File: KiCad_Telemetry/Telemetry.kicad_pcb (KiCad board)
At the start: 2 copper layers, 67 x 51 mm, 38 parts, among them IC1 TCAN1044VDRQ1, J2 Conn_01x03, J3 PinHeader_01x02, J4 PinHeader_01x02, J5 PinHeader_01x02, J7 DB9_Female, J8 USB_A Connector, U1 NRF24L01_Breakout, U2 STM32F042C4T6, U3 TLV70033_SOT23-5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

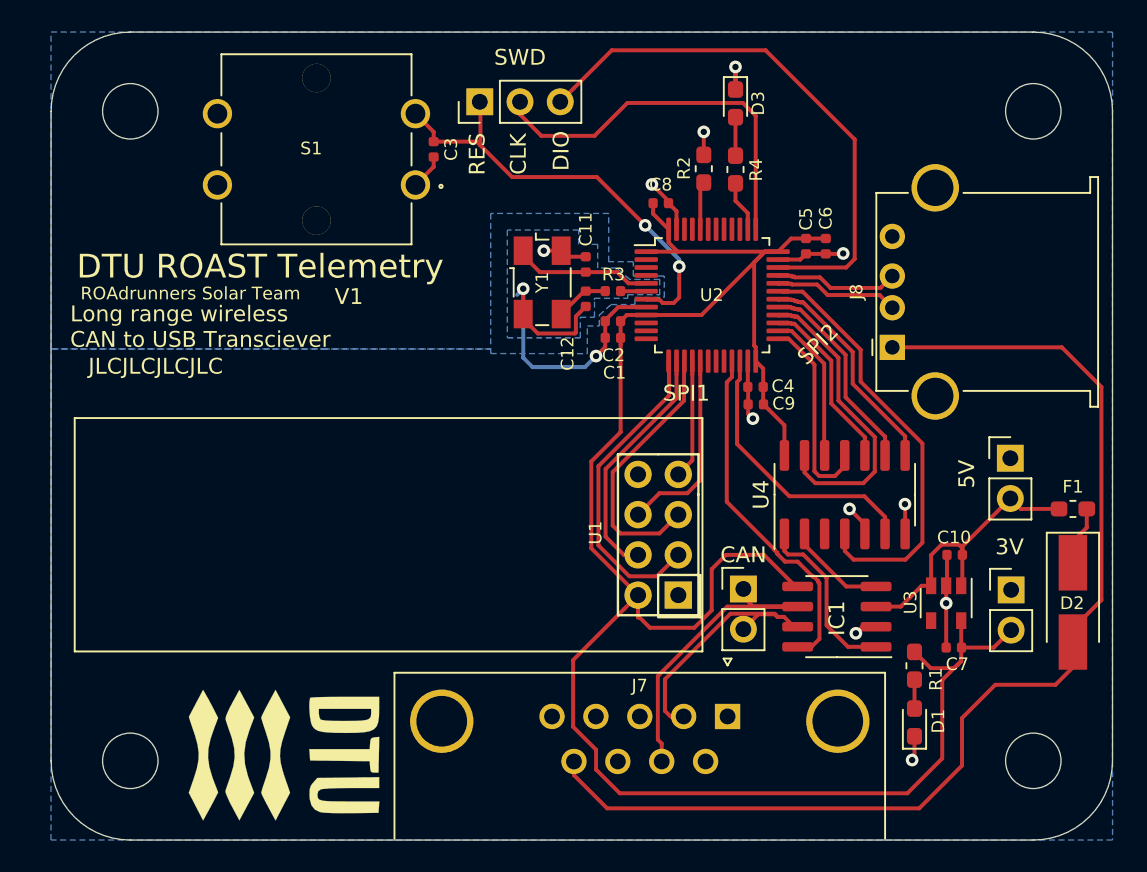
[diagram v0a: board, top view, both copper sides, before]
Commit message: Revised layout, Created GERBER and Drill Files. Finished BOM
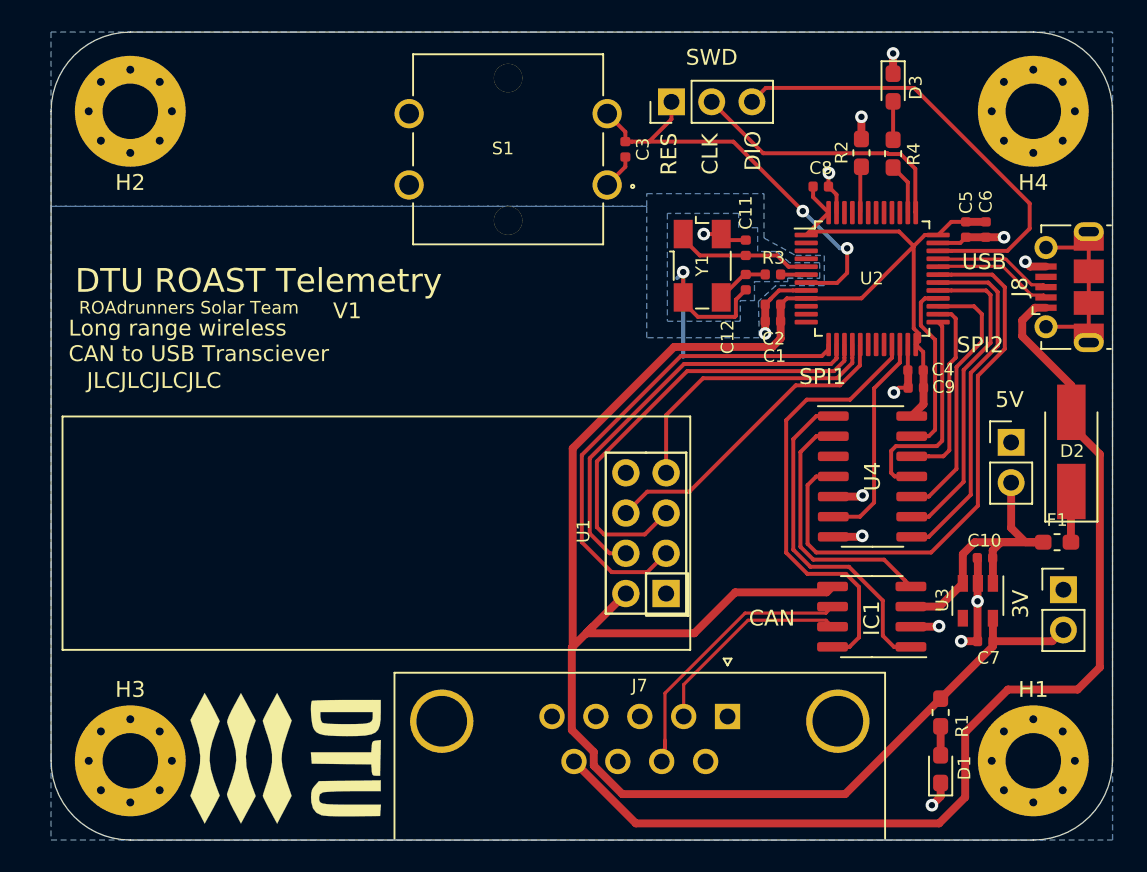
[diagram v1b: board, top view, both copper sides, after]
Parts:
- removed J5: PinHeader_01x02, Connector_PinHeader_2.54mm:PinHeader_1x02_P2.54mm_Vertical
- H1, H2, H3, H4: footprint MountingHole:MountingHole_3.5mm -> MountingHole:MountingHole_3.5mm_Pad_Via
- J8: value USB_A Connector -> USB Micro Connector; footprint Connector_USB:USB_A_Stewart_SS-52100-001_Horizontal -> Connector_USB:USB_Micro-B_Molex-105017-0001
- moved C3 12.1 mm to (219.2, 106.4)
- moved J2 12.1 mm to (222.2, 103.4)
- moved S1 12.1 mm to (211.8, 106.4)
- moved J8 11.8 mm to (247.3, 115.1)
- moved C1 10.2 mm to (228.6, 117.2)
- moved C11 10.2 mm to (226.8, 112.6)
- moved C12 10.2 mm to (226.8, 114.8)
- moved C2 10.2 mm to (228.6, 116.2)
- moved C4 10.2 mm to (237.6, 120.3)
- moved C5 10.2 mm to (240.8, 111.5)
- moved C6 10.2 mm to (242.0, 111.5)
- moved C8 10.2 mm to (231.6, 108.8)
- moved C9 10.2 mm to (237.6, 121.5)
- moved R3 10.2 mm to (228.6, 114.3)
- moved U2 10.2 mm to (234.8, 114.6)
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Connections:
- net USB_DM renamed USB_D-
- net USB_DP renamed USB_D+
- H1 pad 1: (no net) -> GND
- H2 pad 1: (no net) -> GND
- H3 pad 1: (no net) -> GND
- H4 pad 1: (no net) -> GND
- J8 pad 4: GND -> Net-(J8-Pad4)
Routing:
- net Net-(J8-Pad6): track 0.00 -> 13.6 mm
- net SPI1_SCK: track 17.1 -> 28.6 mm
- net SPI1_NSS: track 15.5 -> 26.6 mm
- net CE_Signal: track 20.4 -> 31.3 mm
- net SPI1_MISO: track 7.52 -> 17.9 mm
- net CAN_TX: track 11.4 -> 21.4 mm
- net CAN_RX: track 6.53 -> 16.5 mm
- net INT1: track 27.2 -> 36.8 mm
- net INT3: track 14.0 -> 22.3 mm
- net SPI2_NSS: track 19.2 -> 11.3 mm
- net SPI1_MOSI: track 12.3 -> 20.0 mm
- net INT2: track 12.9 -> 20.1 mm
- net SW_CLK: track 24.6 -> 17.4 mm
- net SW_DIO: track 34.9 -> 28.9 mm
- net SPI2_SCK: track 11.2 -> 16.9 mm
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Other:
- net class Power added: clearance 0.2, trace_width 0.5, via_dia 0.8, via_drill 0.4
- net class Signal added: clearance 0.2, trace_width 0.25, via_dia 0.8, via_drill 0.4
- net class USB added: clearance 0.2, trace_width 0.25, via_dia 0.8, via_drill 0.4
- rule via_min_size: 0.4 -> 0.6
- board text added: "USB"

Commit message: Minor edits; Generated gerber files
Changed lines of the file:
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@@
     (0 F.Cu signal)
     (31 B.Cu signal)
-    (32 B.Adhes user)
-    (33 F.Adhes user)
-    (34 B.Paste user)
-    (35 F.Paste user)
+    (32 B.Adhes user hide)
+    (33 F.Adhes user hide)
+    (34 B.Paste user hide)
+    (35 F.Paste user hide)
     (36 B.SilkS user)
     (37 F.SilkS user)
-    (38 B.Mask user)
-    (39 F.Mask user)
-    (40 Dwgs.User user)
+    (38 B.Mask user hide)
+    (39 F.Mask user hide)
+    (40 Dwgs.User user hide)
     (41 Cmts.User user)
     (42 Eco1.User user)
     (43 Eco2.User user)
     (44 Edge.Cuts user)
-    (45 Margin user)
+    (45 Margin user hide)
     (46 B.CrtYd user)
     (47 F.CrtYd user)
-    (48 B.Fab user)
-    (49 F.Fab user)
+    (48 B.Fab user hide)
+    (49 F.Fab user hide)
   )
   (setup
@@
     (tags "resistor handsolder")
     (attr smd)
-    (fp_text reference F1 (at 0 1.4 180) (layer F.SilkS)
+    (fp_text reference F1 (at -2.3 0.1 270) (layer F.SilkS)
       (effects (font (size 0.8 0.8) (thickness 0.15)))
     )

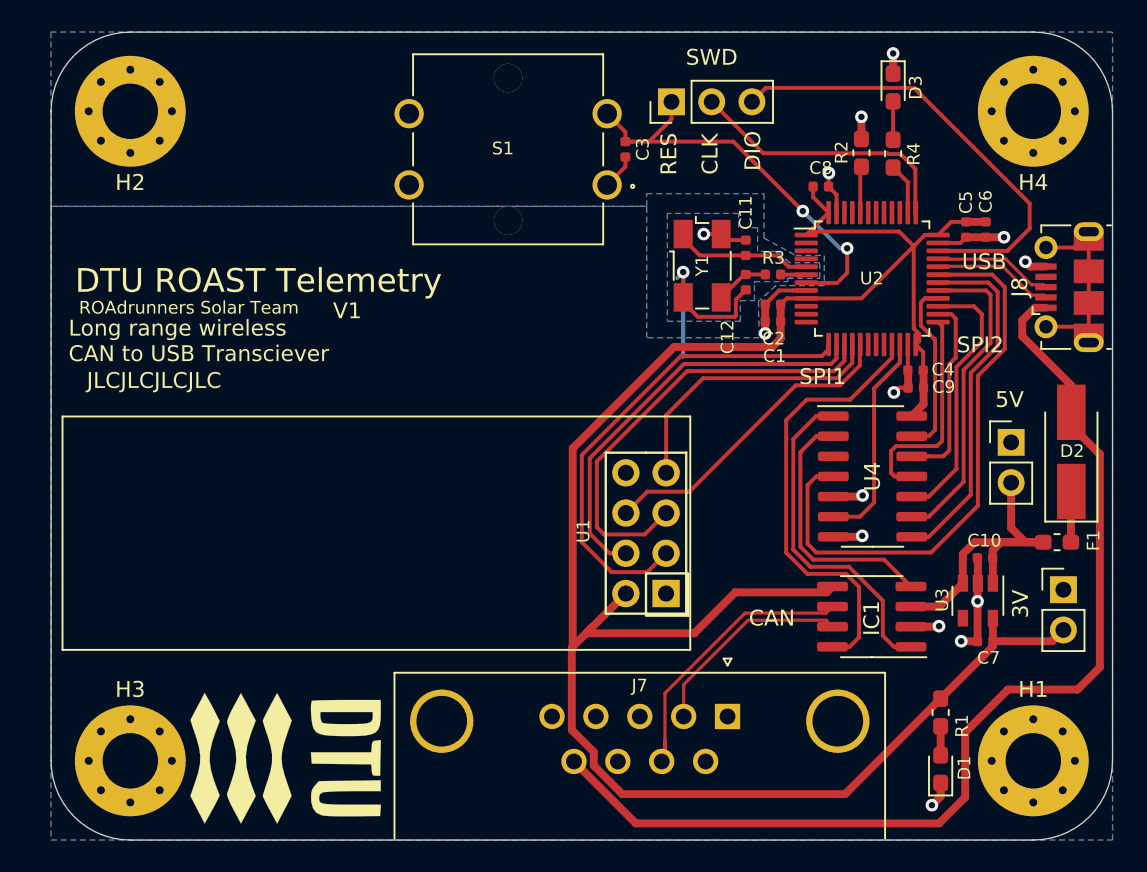
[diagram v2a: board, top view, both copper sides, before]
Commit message: Added additional decoupling capacitors; Added Finished design sent to production
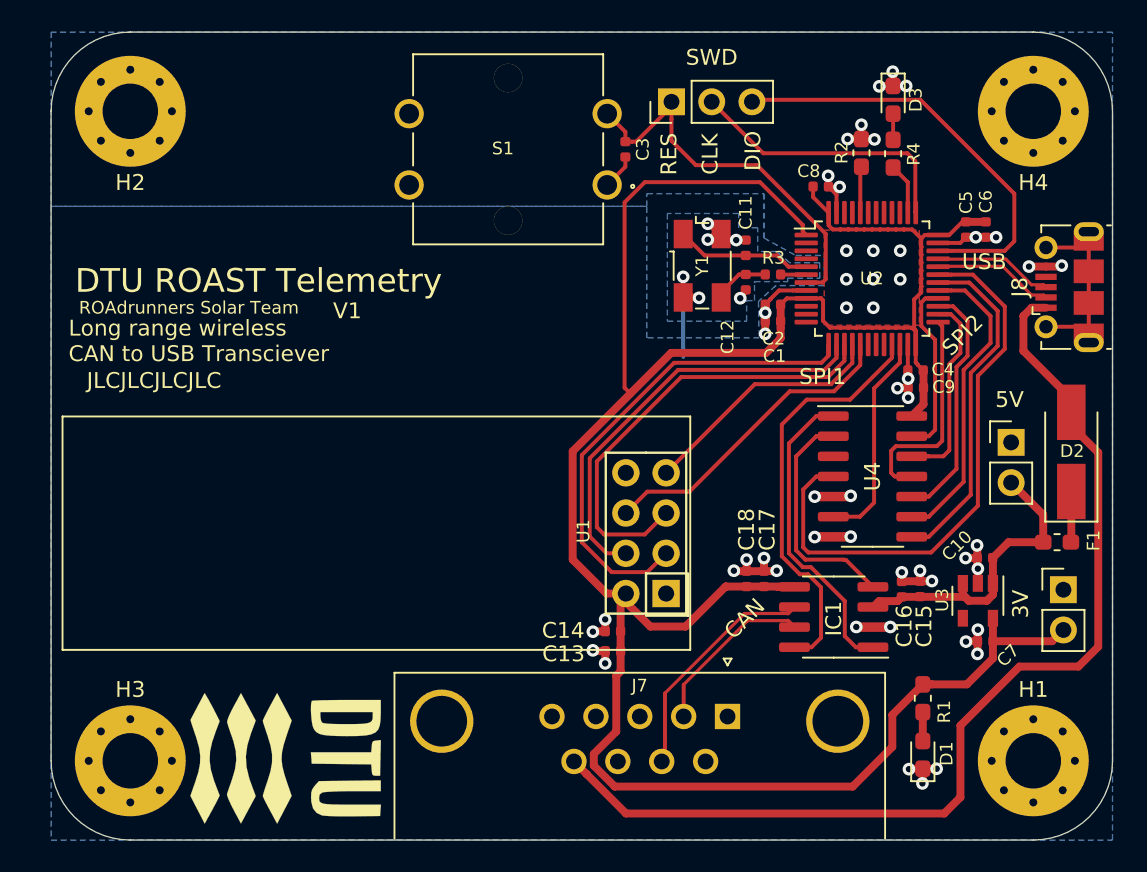
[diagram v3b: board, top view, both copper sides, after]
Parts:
- added C13: 4.7uF, Capacitor_SMD:C_0402_1005Metric, F.Cu at (218.5, 138.1)
- added C14: 100 nF, Capacitor_SMD:C_0402_1005Metric, F.Cu at (218.5, 136.8)
- added C15: 4.7uF, Capacitor_SMD:C_0402_1005Metric, F.Cu at (237.8, 134.2)
- added C16: 100 nF, Capacitor_SMD:C_0402_1005Metric, F.Cu at (236.7, 134.2)
- added C17: 100 nF, Capacitor_SMD:C_0402_1005Metric, F.Cu at (228.0, 133.5)
- added C18: 4.7uF, Capacitor_SMD:C_0402_1005Metric, F.Cu at (226.9, 133.5)
- moved IC1 2.40 mm to (232.4, 135.9)
- moved D1 1.44 mm to (238.0, 144.6)
- moved R1 1.44 mm to (238.0, 141.1)
- moved D3 0.78 mm to (236.2, 103.3)
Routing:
- net +3V3: track 135.0 -> 155.2 mm
- net GND: track 51.6 -> 64.7 mm, vias 15 -> 57
- net CAN-: track 17.2 -> 14.8 mm
- net CAN+: track 13.3 -> 10.8 mm
- net SPI1_MISO: track 17.9 -> 15.8 mm
- net +5V: track 21.9 -> 19.9 mm
- net CAN_STB: track 28.1 -> 26.2 mm
- net CAN_TX: track 21.4 -> 19.5 mm
- net CAN_RX: track 16.5 -> 14.6 mm
- net SW_DIO: track 28.9 -> 27.1 mm
- net SPI2_SCK: track 16.9 -> 15.4 mm
- net Reset: track 26.5 -> 25.2 mm, vias 2 -> 0
- net VCC: track 67.1 -> 65.9 mm
- net INT2: track 20.1 -> 19.3 mm
- net Net-(D3-Pad2): track 2.42 -> 1.65 mm
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- added copper zone on F.Cu, net GND

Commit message: Added Ferrite bead VBUS filtering Replaced LDO with component found on RS-Online (Same footprint, better parameters)
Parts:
- added C19: 10nF, Capacitor_SMD:C_0402_1005Metric, F.Cu at (239.1, 136.6)
- added FB1: Ferrite_Bead, Inductor_SMD:L_0603_1608Metric_Pad1.05x0.95mm_HandSolder, F.Cu at (243.4, 130.6)
- J8: footprint Connector_USB:USB_Micro-B_Molex-105017-0001 -> Connector_USB:USB_Micro-B_Molex_47346-0001
- U3: value TLV70033_SOT23-5 -> LD3985M33R_SOT23
- moved F1 0.52 mm to (247.0, 131.1)
- moved U3 0.13 mm to (241.5, 135.0)
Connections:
- F1 pad 2: +5V -> Net-(F1-Pad2)
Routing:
- net GND: track 64.7 -> 70.7 mm, vias 57 -> 60
- net +5V: track 19.9 -> 15.7 mm
- net +3V3: track 155.2 -> 157.6 mm
- net Net-(F1-Pad2): track 0.00 -> 2.02 mm
- net Net-(J8-Pad6): track 13.6 -> 11.6 mm
- net Net-(C19-Pad2): track 0.00 -> 1.41 mm
- net SPI2_MOSI: track 13.9 -> 15.0 mm
- net INT3: track 21.6 -> 20.9 mm
- net INT2: track 19.3 -> 18.6 mm
- net INT1: track 36.6 -> 35.9 mm
- net VCC: track 65.9 -> 65.3 mm

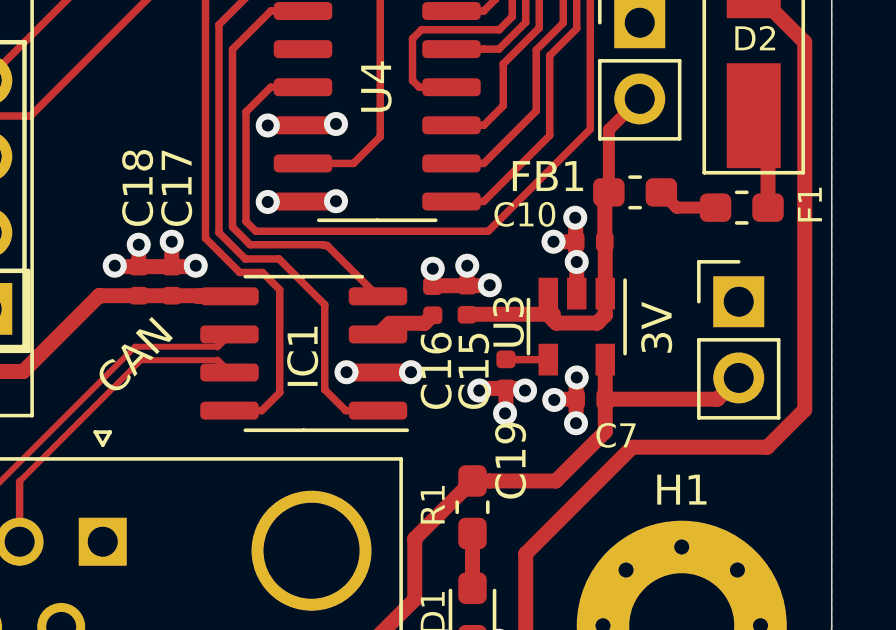
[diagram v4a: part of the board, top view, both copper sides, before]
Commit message: Fixed missing trace
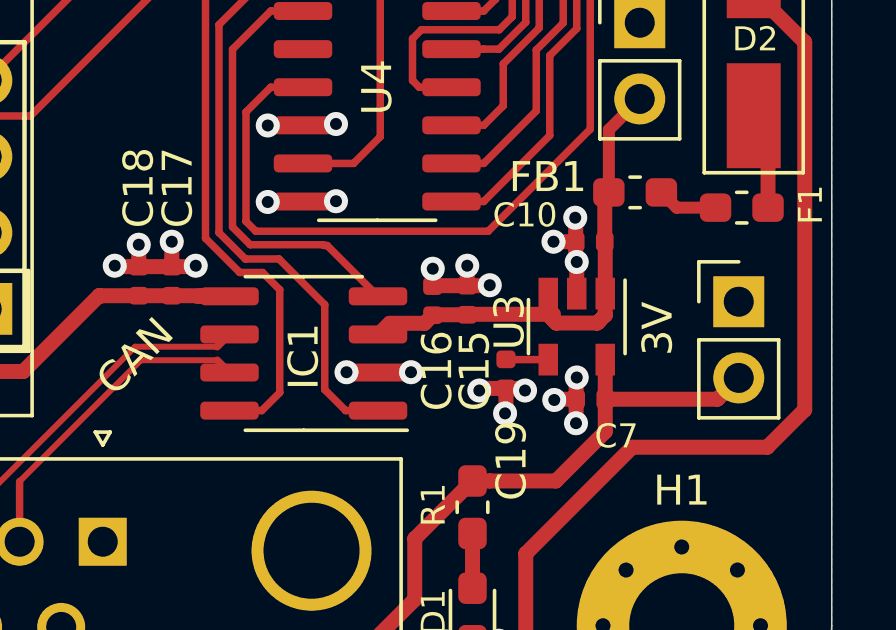
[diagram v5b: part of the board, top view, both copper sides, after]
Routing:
- net +5V: track 15.7 -> 16.8 mm
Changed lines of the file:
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@@
     (thickness 1.6)
     (drawings 23)
-    (tracks 602)
+    (tracks 604)
     (zones 0)
     (modules 45)
@@
   (segment (start 240.724999 134.62) (end 237.865 134.62) (width 0.5) (layer F.Cu) (net 6))
   (segment (start 240.814999 134.910001) (end 240.724999 134.820001) (width 0.5) (layer F.Cu) (net 6))
+  (segment (start 236.715 134.635) (end 236.7 134.65) (width 0.5) (layer F.Cu) (net 6))
+  (segment (start 237.85 134.635) (end 236.715 134.635) (width 0.5) (layer F.Cu) (net 6))
   (segment (start 231.3 123.24) (end 232.375 123.24) (width 0.25) (layer F.Cu) (net 7))
   (segment (start 229.574978 131.8978) (end 229.574978 124.965022) (width 0.25) (layer F.Cu) (net 7))

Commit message: Updated final files for hand-in
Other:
- board text added: "IO"
- board text removed: "DIO"
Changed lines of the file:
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@@
     (effects (font (size 1 1) (thickness 0.15)))
   )
-  (gr_text DIO (at 227.3 106.5 90) (layer F.SilkS)
+  (gr_text IO (at 227.3 106.5 90) (layer F.SilkS)
     (effects (font (size 1 1) (thickness 0.15)))
   )
